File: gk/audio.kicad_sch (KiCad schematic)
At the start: 20 parts, among them J5 AudioJack3_SwitchTR, J6 Conn_01x02, J7 Conn_01x02, U7 PCM1754DBQ, U8 PAM8008

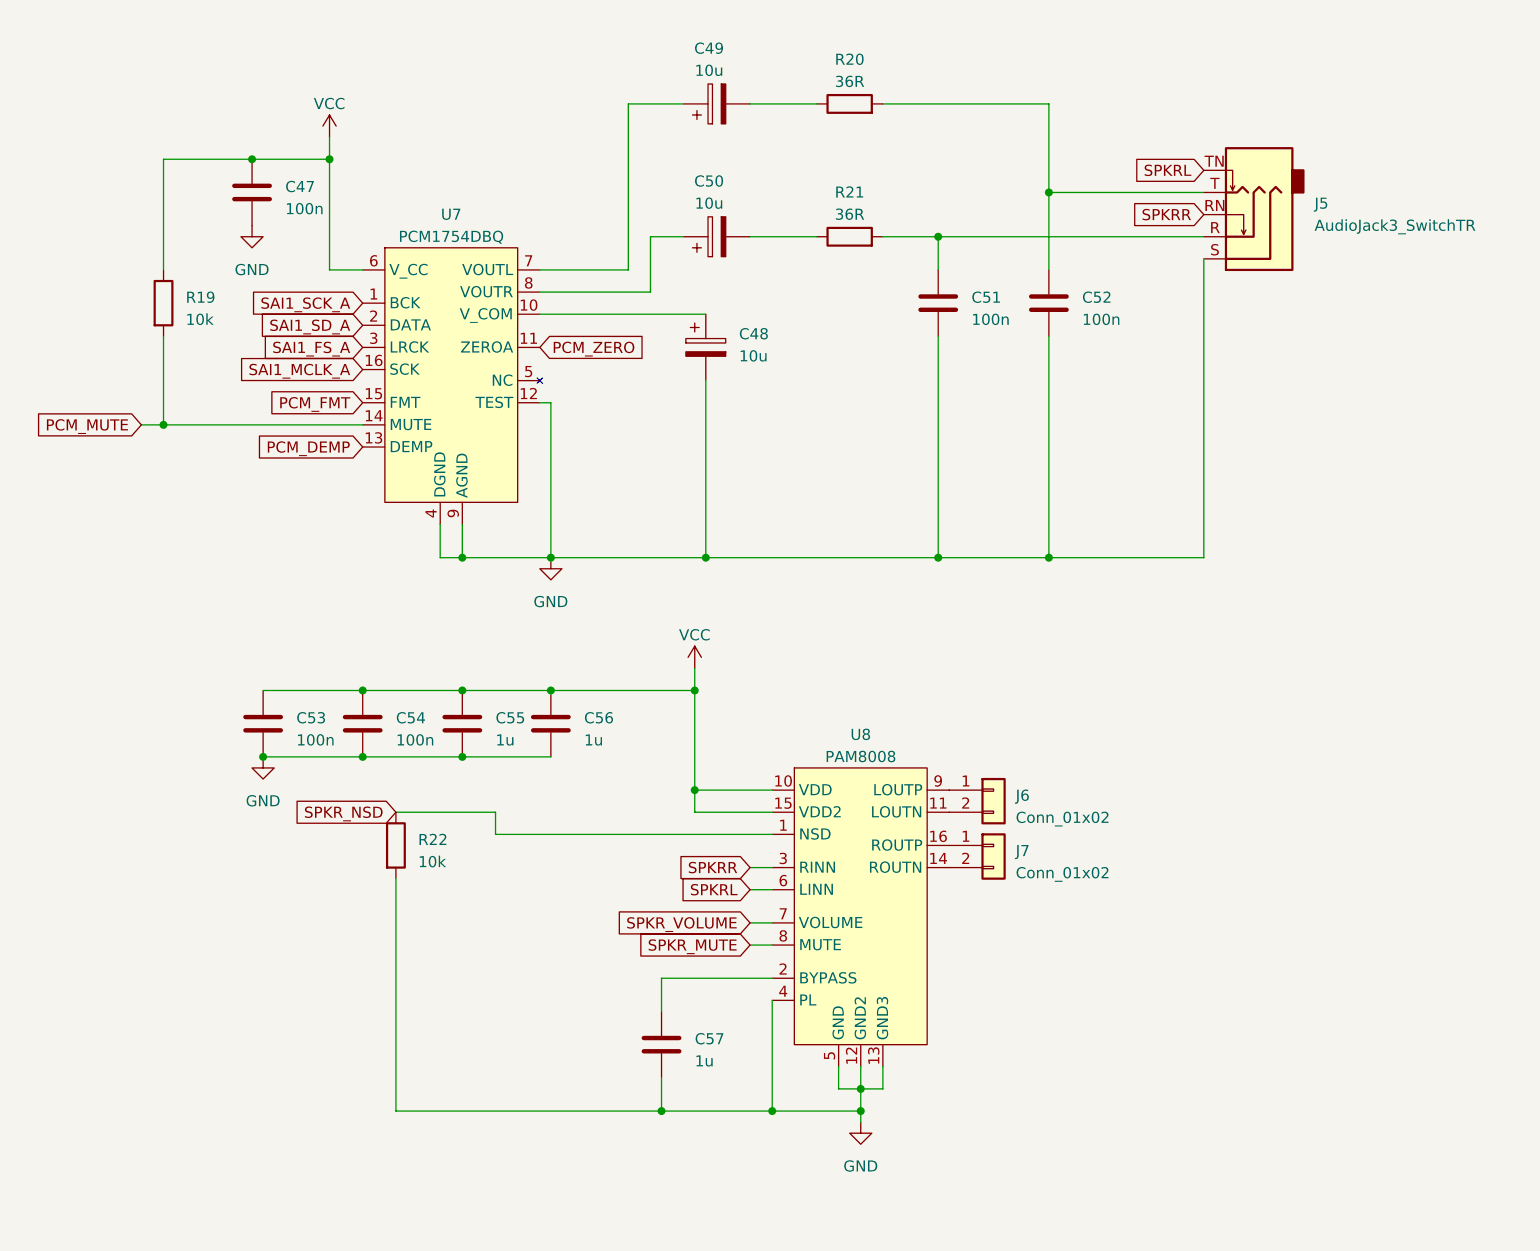
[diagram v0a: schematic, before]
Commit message: Switch speaker amplifier to mono
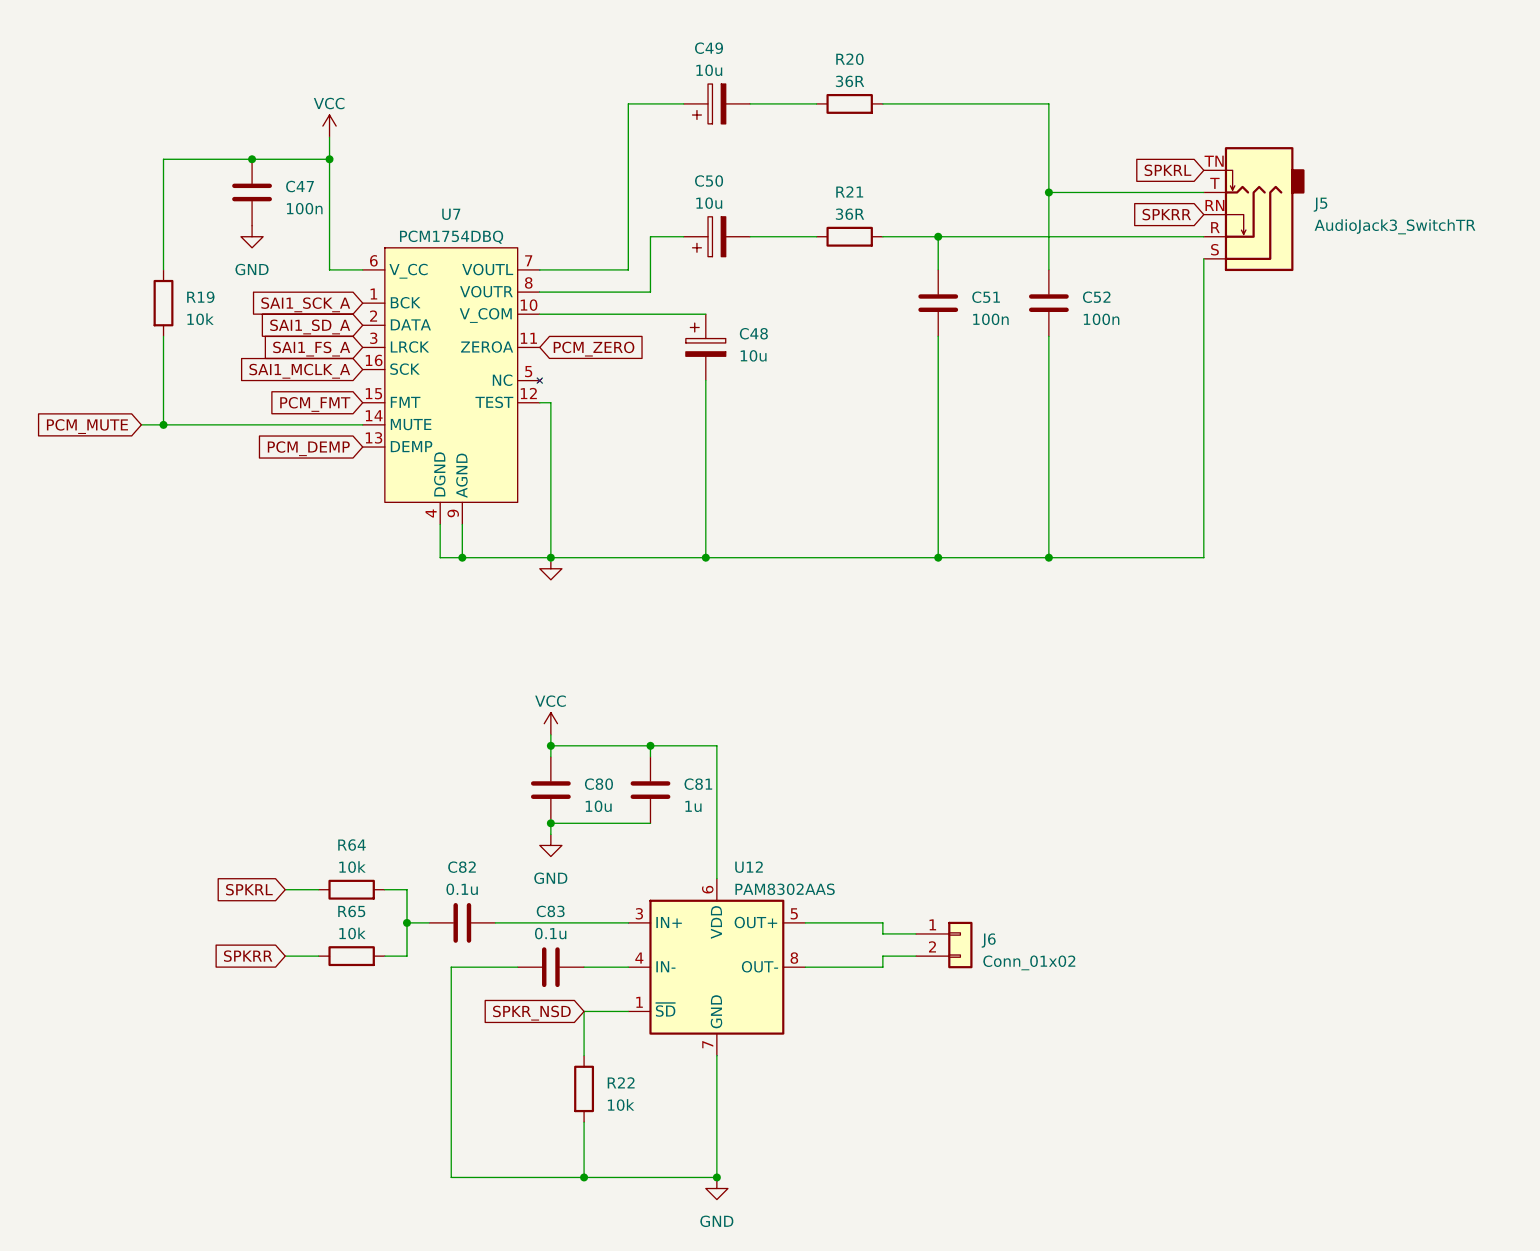
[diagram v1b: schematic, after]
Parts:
- removed C53, C54: 100n, Capacitor_SMD:C_0603_1608Metric, symbol Device:C
- removed C55, C56, C57: 1u, Capacitor_SMD:C_0805_2012Metric, symbol Device:C
- removed J7: Conn_01x02, Connector_Molex:Molex_PicoBlade_53048-0210_1x02_P1.25mm_Horizontal, symbol Connector_Generic:Conn_01x02
- removed U8: PAM8008, Package_SO:SOP-16_3.9x9.9mm_P1.27mm, symbol gk-syms:PAM8008
- added C80: 10u, Capacitor_SMD:C_0805_2012Metric, symbol Device:C
- added C81: 1u, Capacitor_SMD:C_0805_2012Metric, symbol Device:C
- added C82, C83: 0.1u, Capacitor_SMD:C_0603_1608Metric, symbol Device:C
- added R64, R65: 10k, Resistor_SMD:R_0603_1608Metric, symbol Device:R
- added U12: PAM8302AAS, Package_SO:MSOP-8_3x3mm_P0.65mm, symbol Amplifier_Audio:PAM8302AAS
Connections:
- net GND: now also C80.2, C81.2, C83.2, U12.7 (GND)
- net SPKRL: now also R64.1
- net SPKRR: now also R65.1
- net SPKR_NSD: now also U12.1 (~{SD})
- net VCC: now also C80.1, C81.1, U12.6 (VDD)
- net at J6.2 (Pin_2): now also U12.8 (OUT-)
- net at J6.1 (Pin_1): now also U12.5 (OUT+)
- new net: C82.1, U12.3 (IN+)
- new net: C83.1, U12.4 (IN-)
- new net: C82.2, R64.2, R65.2

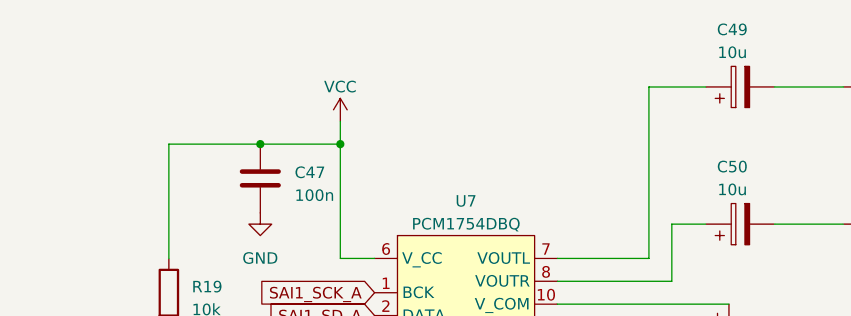
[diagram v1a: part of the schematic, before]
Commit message: consider hardware volume control
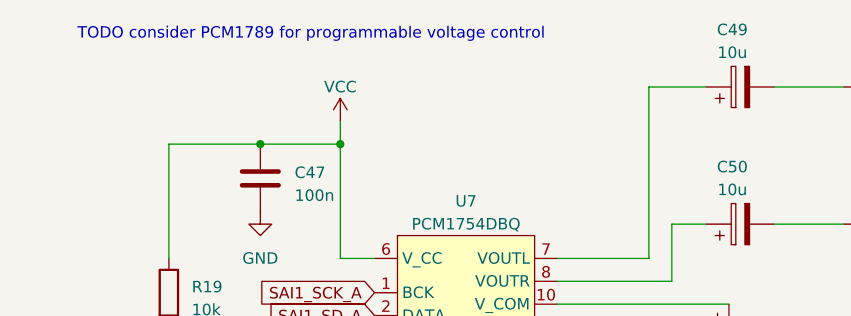
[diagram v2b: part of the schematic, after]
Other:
- note added: "TODO consider PCM1789 for programmable voltage control"
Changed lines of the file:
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@@
     (stroke (width 0) (type default))
+  )
+  (text "TODO consider PCM1789 for programmable voltage control"
+    (at 39.37 21.59 0)
+    (effects (font (size 1.27 1.27)) (justify left bottom))
   )
   (global_label "SAI1_SCK_A" (shape input) (at 72.39 49.53 180) (fields_autoplaced)

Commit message: update gamepad buttons
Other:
- note added: "TODO needs ferrite bead between VCC and AVCC"
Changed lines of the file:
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@@
+    (effects (font (size 1.27 1.27)) (justify left bottom))
+  )
+  (text "TODO needs ferrite bead between VCC and AVCC" (at 39.37 24.13 0)
     (effects (font (size 1.27 1.27)) (justify left bottom))
   )

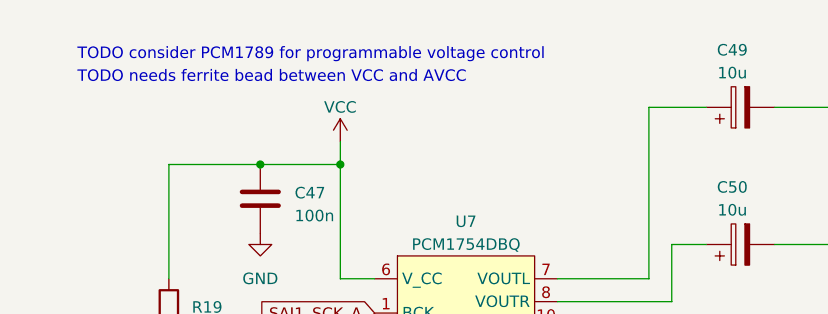
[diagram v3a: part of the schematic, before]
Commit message: add extra todo about output stage
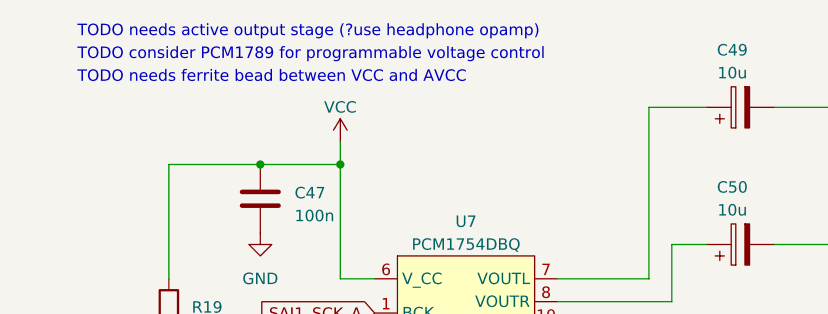
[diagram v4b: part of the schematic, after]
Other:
- note added: "TODO needs active output stage (?use headphone opamp)"
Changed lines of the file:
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@@
+    (effects (font (size 1.27 1.27)) (justify left bottom))
+  )
+  (text "TODO needs active output stage (?use headphone opamp)"
+    (at 39.37 19.05 0)
     (effects (font (size 1.27 1.27)) (justify left bottom))
   )

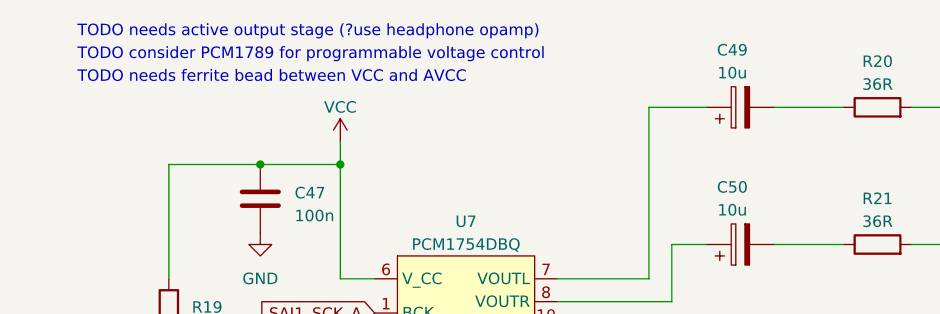
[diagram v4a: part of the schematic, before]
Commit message: suggestion for headphone amp
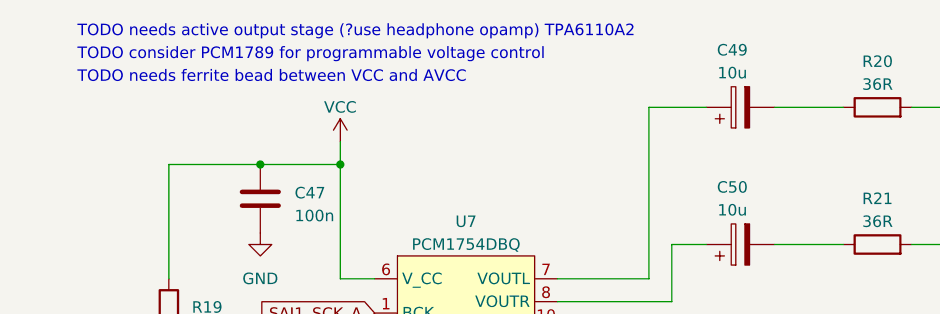
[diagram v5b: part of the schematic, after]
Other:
- note added: "TODO needs active output stage (?use headphone opamp) TPA6110A2"
- note removed: "TODO needs active output stage (?use headphone opamp)"
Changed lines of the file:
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@@
     (effects (font (size 1.27 1.27)) (justify left bottom))
   )
-  (text "TODO needs active output stage (?use headphone opamp)"
+  (text "TODO needs active output stage (?use headphone opamp) TPA6110A2"
     (at 39.37 19.05 0)
     (effects (font (size 1.27 1.27)) (justify left bottom))
